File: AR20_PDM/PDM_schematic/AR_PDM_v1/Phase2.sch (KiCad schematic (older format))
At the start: 15 parts, among them Q1 BTS50025-1TAD, U1 INA233

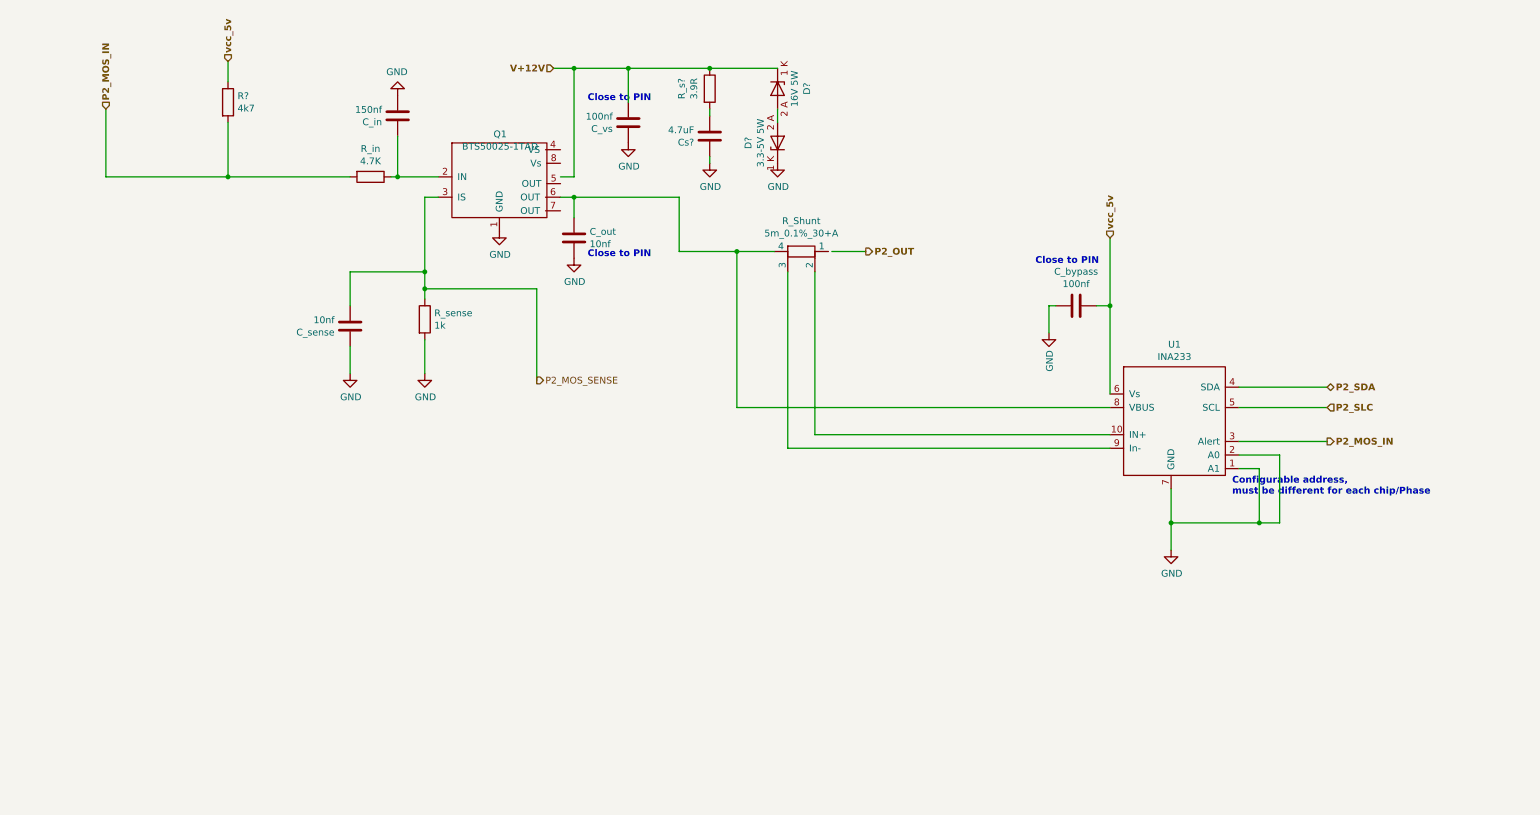
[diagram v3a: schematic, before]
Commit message: Fixed issues, controlled components, BOM, see discription
- added acm symbol
- fixed wrongly faced P-mosfets
- I/O expander now sinks led instead of source
- Bill of material mostly done
- Correct address for INA233 chips.
- Now 4 diodes serves as flyback for all mosfets
- Corrected naming scheme for compmonents (everything is not fixed yet)
- Fixed some labels
- altso some minor changes
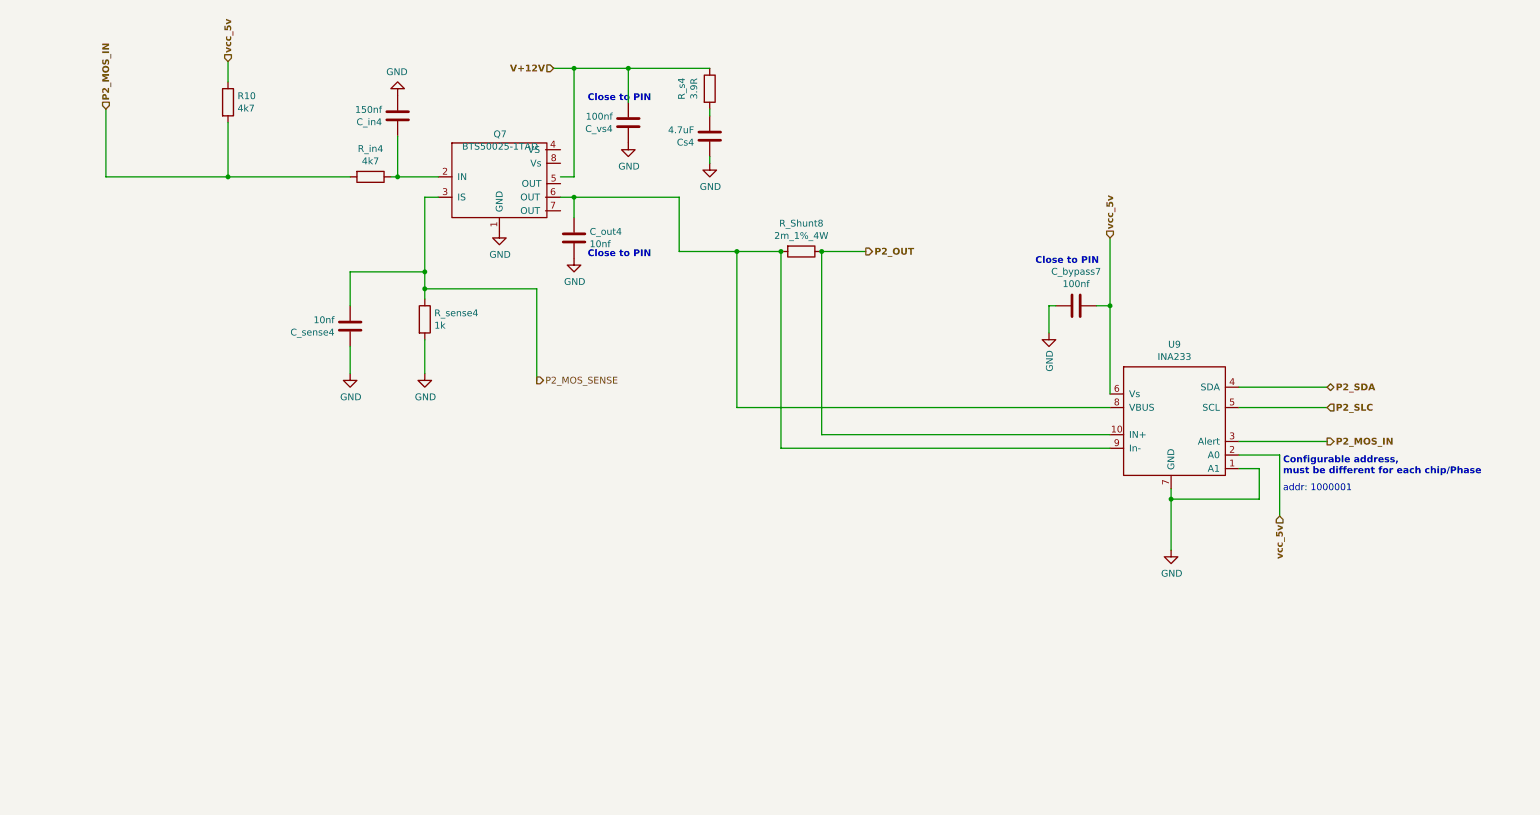
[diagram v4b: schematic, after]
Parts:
- removed C_in: 150nf, symbol AR20_PDM_v1-rescue:C-Device
- removed C_out, C_sense: 10nf, symbol AR20_PDM_v1-rescue:C-Device
- removed C_vs: 100nf, symbol AR20_PDM_v1-rescue:C-Device
- removed Cs?: 4.7uF, symbol AR20_PDM_v1-rescue:C-Device
- removed D?: 3.3-5V 5W, symbol AR20_PDM_v1-rescue:D_Zener-Device
- removed D?: 16V 5W, symbol AR20_PDM_v1-rescue:D_Zener-Device
- removed Q1: BTS50025-1TAD, symbol AR20_PDM_v1-rescue:BTS50025-1TAD
- removed R?: 4k7, symbol AR20_PDM_v1-rescue:R-Device
- removed R_Shunt: 5m_0.1%_30+A, symbol AR20_PDM_v1-rescue:R_Shunt-Device
- removed R_in: 4.7K, symbol AR20_PDM_v1-rescue:R-Device
- removed R_s?: 3.9R, symbol AR20_PDM_v1-rescue:R-Device
- removed R_sense: 1k, symbol AR20_PDM_v1-rescue:R-Device
- removed U1: INA233, symbol AR20_PDM_v1-rescue:INA233
- added C_in4: 150nf, Capacitor_SMD:C_0603_1608Metric, symbol AR20_PDM_v1-rescue:C-Device
- added C_out4, C_sense4: 10nf, Capacitor_SMD:C_0603_1608Metric, symbol AR20_PDM_v1-rescue:C-Device
- added C_vs4: 100nf, Capacitor_SMD:C_0603_1608Metric, symbol AR20_PDM_v1-rescue:C-Device
- added Cs4: 4.7uF, Capacitor_SMD:C_1206_3216Metric, symbol AR20_PDM_v1-rescue:C-Device
- added Q7: BTS50025-1TAD, symbol AR20_PDM_v1-rescue:BTS50025-1TAD
- added R10, R_in4: 4k7, symbol AR20_PDM_v1-rescue:R-Device
- added R_Shunt8: 2m_1%_4W, symbol AR20_PDM_v1-rescue:R-Device
- added R_s4: 3.9R, symbol AR20_PDM_v1-rescue:R-Device
- added R_sense4: 1k, symbol AR20_PDM_v1-rescue:R-Device
- added U9: INA233, symbol AR20_PDM_v1-rescue:INA233
- C_bypass7: renamed from C_bypass; footprint (none) -> Capacitor_SMD:C_0603_1608Metric
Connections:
- wire segments 57 -> 54
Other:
- note added: "addr: 1000001"

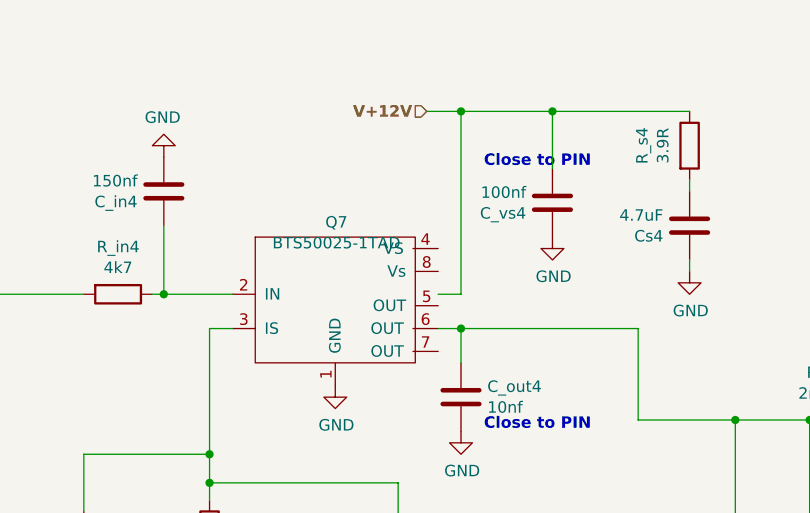
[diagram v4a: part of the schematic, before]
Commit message: PCB design, and issue fixing, work in progress
- Error fixed: Mux mosfet resistor change to ground
- Open drain output added on phase 6, for engine blipping purpose
- Most of pcb symbols and footprints are finished, including main connector
- PCB is change from 1oz to 2oz copper layer, for easier routing.
- Basic Draft of pcb is done, for now.
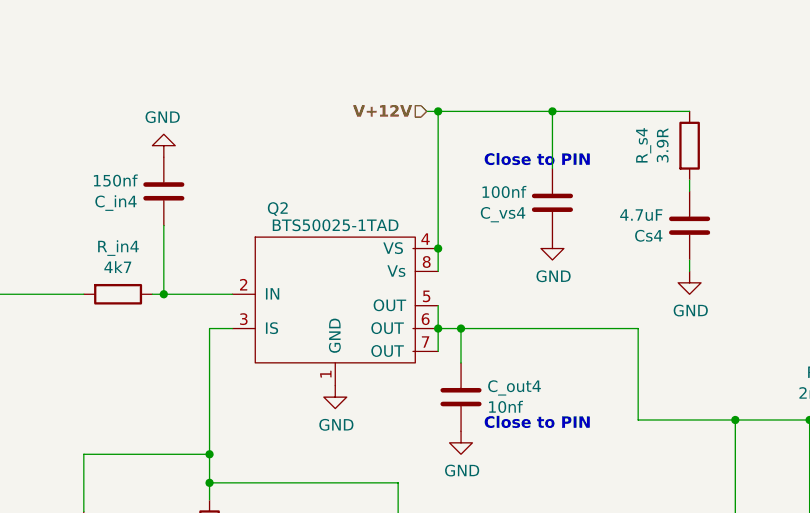
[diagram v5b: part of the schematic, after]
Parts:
- Q2: renamed from Q7; footprint (none) -> AR_PDM_v1:BTS500xx
- R10, R_in4, R_s4, R_sense4: footprint (none) -> Resistor_SMD:R_0603_1608Metric
- R_Shunt8: footprint (none) -> Resistor_SMD:R_2512_6332Metric
- U9: footprint (none) -> AR_PDM_v1:INA233
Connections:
- net V+12V: now also Q2.4 (VS), Q2.8 (Vs)
- net at C_out4.1, Q2.6 (OUT), R_Shunt8.2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: now also Q2.5 (OUT), Q2.7 (OUT)
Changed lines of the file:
@@
 F 0 "R_in4" V 3093 2400 50  0000 C CNN
 F 1 "4k7" V 3184 2400 50  0000 C CNN
-F 2 "" V 3230 2400 50  0001 C CNN
+F 2 "Resistor_SMD:R_0603_1608Metric" V 3230 2400 50  0001 C CNN
 F 3 "~" H 3300 2400 50  0001 C CNN
 	1    3300 2400
@@
 F 0 "R10" H 2320 1896 50  0000 L CNN
 F 1 "4k7" H 2320 1805 50  0000 L CNN
-F 2 "" V 2180 1850 50  0001 C CNN
+F 2 "Resistor_SMD:R_0603_1608Metric" V 2180 1850 50  0001 C CNN
 F 3 "~" H 2250 1850 50  0001 C CNN
 	1    2250 1850
@@
 AR Path="/5E0E594B/5E21B7FD" Ref="Q?"  Part="1"
 AR Path="/5E0E607C/5E21B7FD" Ref="Q?"  Part="1"
-AR Path="/5E0FB5C8/5E21B7FD" Ref="Q7"  Part="1"
+AR Path="/5E0FB5C8/5E21B7FD" Ref="Q2"  Part="1"
 AR Path="/5E0FBBBD/5E21B7FD" Ref="Q?"  Part="1"
 AR Path="/5E0FC3A2/5E21B7FD" Ref="Q?"  Part="1"
@@
 AR Path="/5E0FDCCC/5E21B7FD" Ref="Q?"  Part="1"
 AR Path="/5E10174B/5E21B7FD" Ref="Q?"  Part="1"
-F 0 "Q7" H 4255 3215 50  0000 C CNN
-F 1 "BTS50025-1TAD" H 4255 3124 50  0000 C CNN
-F 2 "" H 4250 2650 50  0001 C CNN
+F 0 "Q2" H 4000 3275 50  0000 C CNN
+F 1 "BTS50025-1TAD" H 4250 3200 50  0000 C CNN
+F 2 "AR_PDM_v1:BTS500xx" H 4250 2650 50  0001 C CNN
 F 3 "" H 4250 2650 50  0001 C CNN
 	1    4250 2650
@@
 F 0 "U9" H 9225 4465 50  0000 C CNN
 F 1 "INA233" H 9225 4374 50  0000 C CNN
-F 2 "" H 9200 4050 50  0001 C CNN
+F 2 "AR_PDM_v1:INA233" H 9200 4050 50  0001 C CNN
 F 3 "" H 9200 4050 50  0001 C CNN
 	1    9200 4050
@@
 Wire Wire Line
 	3700 3100 3700 3225
-Wire Wire Line
-	4700 2400 4800 2400
-Wire Wire Line
-	4800 2400 4800 1600
-Wire Wire Line
-	4800 1600 4650 1600
 Text HLabel 2250 1550 1    50   Input ~ 10
 vcc_5v
@@
 F 0 "R_s4" V 5593 1750 50  0000 C CNN
 F 1 "3.9R" V 5684 1750 50  0000 C CNN
-F 2 "" V 5730 1750 50  0001 C CNN
+F 2 "Resistor_SMD:R_0603_1608Metric" V 5730 1750 50  0001 C CNN
 F 3 "~" H 5800 1750 50  0001 C CNN
 	1    5800 1750
@@
 Wire Wire Line
 	5200 1600 5800 1600
-Wire Wire Line
-	4800 1600 5200 1600
-Connection ~ 4800 1600
 Connection ~ 5200 1600
 Text HLabel 1350 1900 1    50   Input ~ 10
@@
 F 0 "R_sense4" H 3770 3496 50  0000 L CNN
 F 1 "1k" H 3770 3405 50  0000 L CNN
-F 2 "" V 3630 3450 50  0001 C CNN
+F 2 "Resistor_SMD:R_0603_1608Metric" V 3630 3450 50  0001 C CNN
 F 3 "~" H 3700 3450 50  0001 C CNN
 	1    3700 3450
@@
 F 0 "R_Shunt8" V 6268 2950 50  0000 C CNN
 F 1 "2m_1%_4W" V 6359 2950 50  0000 C CNN
-F 2 "" V 6405 2950 50  0001 C CNN
+F 2 "Resistor_SMD:R_2512_6332Metric" V 6405 2950 50  0001 C CNN
 F 3 "~" H 6475 2950 50  0001 C CNN
 	1    6475 2950
@@
 Text HLabel 10000 4900 3    50   Input ~ 10
 vcc_5v
+Wire Wire Line
+	4650 1600 4700 1600
+Wire Wire Line
+	4700 2300 4700 2200
+Wire Wire Line
+	4700 2200 4700 1600
+Connection ~ 4700 2200
+Connection ~ 4700 1600
+Wire Wire Line
+	4700 1600 5200 1600
+Connection ~ 4700 2550
+Wire Wire Line
+	4700 2450 4700 2550
+Wire Wire Line
+	4700 2650 4700 2550
 $EndSCHEMATC

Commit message: PCB Design, Work in progress
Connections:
- net P2_Shunt: now reaches C_out4.1, Q2.5 (OUT), Q2.6 (OUT), Q2.7 (OUT), R_Shunt8.2, U9.8 (VBUS), U9.9 (In-)
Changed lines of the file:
@@
 $Descr A4 11693 8268
 encoding utf-8
-Sheet 8 13
+Sheet 7 13
 Title ""
 Date ""
@@
 Wire Wire Line
 	4700 2650 4700 2550
+Wire Wire Line
+	6000 2950 6000 2825
+Text HLabel 6000 2825 1    50   Input ~ 0
+P2_Shunt
 $EndSCHEMATC

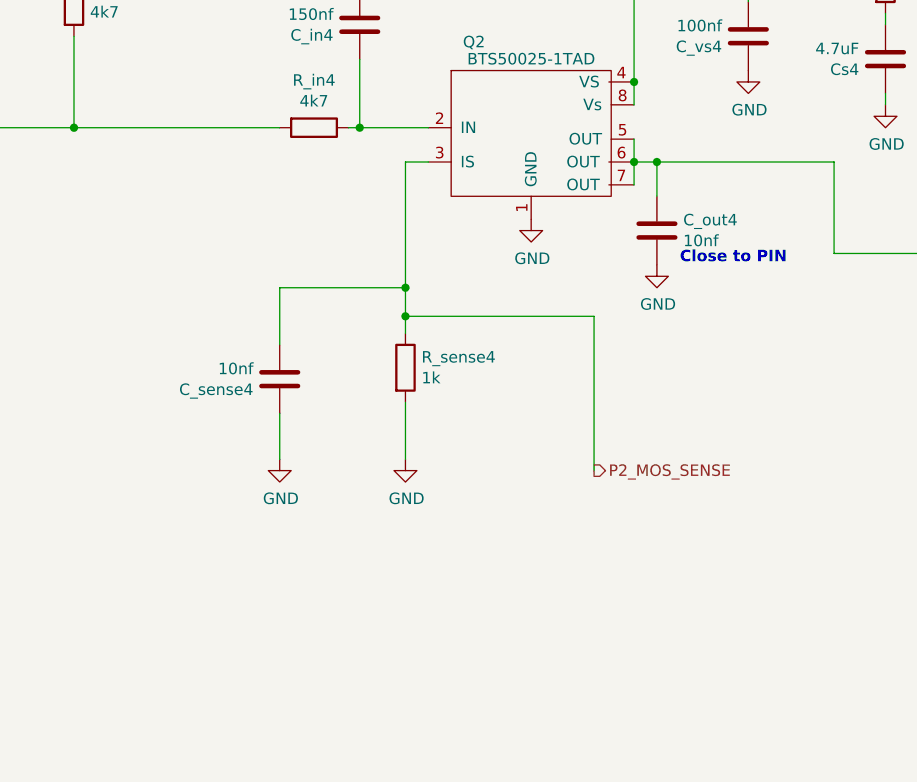
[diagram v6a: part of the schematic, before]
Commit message: PCB Design,  minor schematics changes, work in progress, see description
- Removed mos sense caps and resistors accept one, 
since only one measurement can be done, at a time.
- added mos sens protection resistors on each line, to protect mux mosfets and micro controller. 
- Routing plan mostly finalized, some of the traces are just proof of concept.
those needs to be routed nicely.
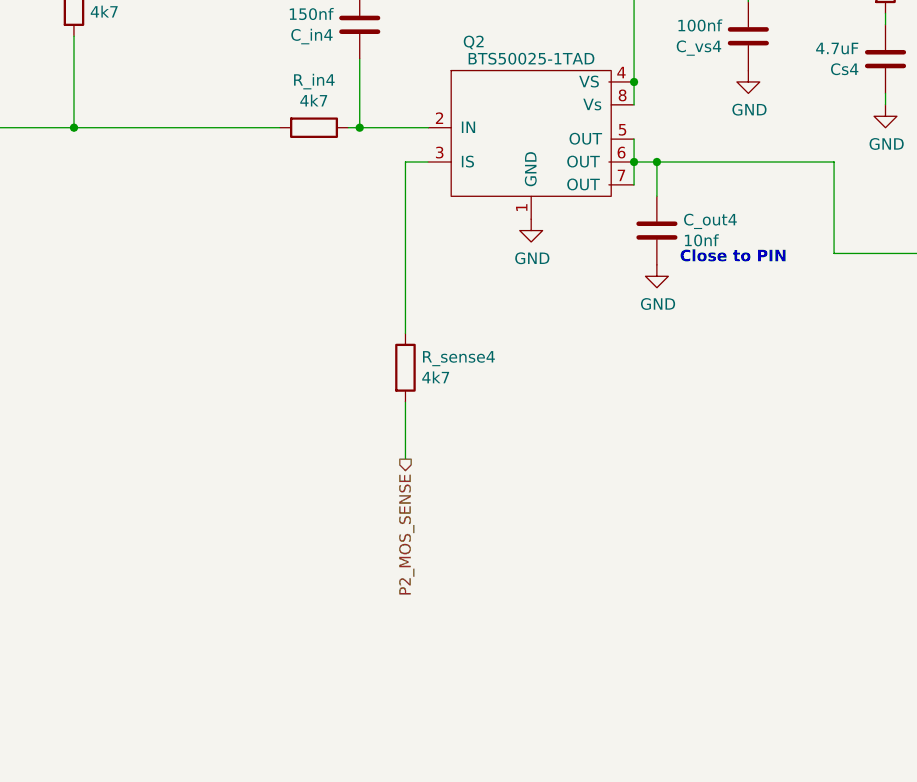
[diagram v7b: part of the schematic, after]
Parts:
- removed C_sense4: 10nf, Capacitor_SMD:C_0603_1608Metric, symbol AR20_PDM_v1-rescue:C-Device
- R_sense4: value 1k -> 4k7
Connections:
- net GND: no longer R_sense4.2
- net P2_MOS_SENSE: now also R_sense4.2; no longer Q2.3 (IS), R_sense4.1
- new net: Q2.3 (IS), R_sense4.1
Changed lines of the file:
@@
-$EndComp
-$Comp
-L AR20_PDM_v1-rescue:GND-power #PWR?
-U 1 1 5DAAC1EF
-P 3700 3850
-AR Path="/5DA89415/5DAAC1EF" Ref="#PWR?"  Part="1"
-AR Path="/5DEB10A1/5DAAC1EF" Ref="#PWR?"  Part="1"
-AR Path="/5DEB20EA/5DAAC1EF" Ref="#PWR?"  Part="1"
-AR Path="/5E0E4725/5DAAC1EF" Ref="#PWR?"  Part="1"
-AR Path="/5E0E4A93/5DAAC1EF" Ref="#PWR?"  Part="1"
-AR Path="/5E0E4EB5/5DAAC1EF" Ref="#PWR?"  Part="1"
-AR Path="/5E0E5304/5DAAC1EF" Ref="#PWR?"  Part="1"
-AR Path="/5E0E594B/5DAAC1EF" Ref="#PWR?"  Part="1"
-AR Path="/5E0E607C/5DAAC1EF" Ref="#PWR?"  Part="1"
-AR Path="/5E0FB5C8/5DAAC1EF" Ref="#PWR065"  Part="1"
-AR Path="/5E0FBBBD/5DAAC1EF" Ref="#PWR?"  Part="1"
-AR Path="/5E0FC3A2/5DAAC1EF" Ref="#PWR?"  Part="1"
-AR Path="/5E0FCFDC/5DAAC1EF" Ref="#PWR?"  Part="1"
-AR Path="/5E0FDCCC/5DAAC1EF" Ref="#PWR?"  Part="1"
-AR Path="/5E10174B/5DAAC1EF" Ref="#PWR?"  Part="1"
-F 0 "#PWR065" H 3700 3600 50  0001 C CNN
-F 1 "GND" H 3705 3677 50  0000 C CNN
-F 2 "" H 3700 3850 50  0001 C CNN
-F 3 "" H 3700 3850 50  0001 C CNN
-	1    3700 3850
-	1    0    0    -1
 $EndComp
 $Comp
@@
 $EndComp
 Wire Wire Line
-	3700 2550 3700 3100
-Wire Wire Line
 	3700 2550 3800 2550
 Wire Wire Line
@@
 Wire Wire Line
 	9700 4450 10000 4450
-$Comp
-L AR20_PDM_v1-rescue:GND-power #PWR?
-U 1 1 5E21B84D
-P 3150 3850
-AR Path="/5DA89415/5E21B84D" Ref="#PWR?"  Part="1"
-AR Path="/5DEB10A1/5E21B84D" Ref="#PWR?"  Part="1"
-AR Path="/5DEB20EA/5E21B84D" Ref="#PWR?"  Part="1"
-AR Path="/5E0E4725/5E21B84D" Ref="#PWR?"  Part="1"
-AR Path="/5E0E4A93/5E21B84D" Ref="#PWR?"  Part="1"
-AR Path="/5E0E4EB5/5E21B84D" Ref="#PWR?"  Part="1"
-AR Path="/5E0E5304/5E21B84D" Ref="#PWR?"  Part="1"
-AR Path="/5E0E594B/5E21B84D" Ref="#PWR?"  Part="1"
-AR Path="/5E0E607C/5E21B84D" Ref="#PWR?"  Part="1"
-AR Path="/5E0FB5C8/5E21B84D" Ref="#PWR063"  Part="1"
-AR Path="/5E0FBBBD/5E21B84D" Ref="#PWR?"  Part="1"
-AR Path="/5E0FC3A2/5E21B84D" Ref="#PWR?"  Part="1"
-AR Path="/5E0FCFDC/5E21B84D" Ref="#PWR?"  Part="1"
-AR Path="/5E0FDCCC/5E21B84D" Ref="#PWR?"  Part="1"
-AR Path="/5E10174B/5E21B84D" Ref="#PWR?"  Part="1"
-F 0 "#PWR063" H 3150 3600 50  0001 C CNN
-F 1 "GND" H 3155 3677 50  0000 C CNN
-F 2 "" H 3150 3850 50  0001 C CNN
-F 3 "" H 3150 3850 50  0001 C CNN
-	1    3150 3850
-	1    0    0    -1
-$EndComp
-$Comp
-L AR20_PDM_v1-rescue:C-Device C_sense?
-U 1 1 5E21B853
-P 3150 3500
-AR Path="/5DA89415/5E21B853" Ref="C_sense?"  Part="1"
-AR Path="/5DEB10A1/5E21B853" Ref="C_sense?"  Part="1"
-AR Path="/5DEB20EA/5E21B853" Ref="C_sense?"  Part="1"
-AR Path="/5E0E4725/5E21B853" Ref="C_sense?"  Part="1"
-AR Path="/5E0E4A93/5E21B853" Ref="C_sense?"  Part="1"
-AR Path="/5E0E4EB5/5E21B853" Ref="C_sense?"  Part="1"
-AR Path="/5E0E5304/5E21B853" Ref="C_sense?"  Part="1"
-AR Path="/5E0E594B/5E21B853" Ref="C_sense?"  Part="1"
-AR Path="/5E0E607C/5E21B853" Ref="C_sense?"  Part="1"
-AR Path="/5E0FB5C8/5E21B853" Ref="C_sense4"  Part="1"
-AR Path="/5E0FBBBD/5E21B853" Ref="C_sense?"  Part="1"
-AR Path="/5E0FC3A2/5E21B853" Ref="C_sense?"  Part="1"
-AR Path="/5E0FCFDC/5E21B853" Ref="C_sense?"  Part="1"
-AR Path="/5E0FDCCC/5E21B853" Ref="C_sense?"  Part="1"
-AR Path="/5E10174B/5E21B853" Ref="C_sense?"  Part="1"
-F 0 "C_sense4" H 3265 3546 50  0000 L CNN
-F 1 "10nf" H 3265 3455 50  0000 L CNN
-F 2 "Capacitor_SMD:C_0603_1608Metric" H 3188 3350 50  0001 C CNN
-F 3 "~" H 3150 3500 50  0001 C CNN
-	1    3150 3500
-	-1   0    0    1
-$EndComp
 Wire Wire Line
 	3450 2400 3500 2400
@@
 Text Notes 8200 3050 0    50   ~ 10
 Close to PIN
-Wire Wire Line
-	3150 3100 3150 3350
-Wire Wire Line
-	3150 3650 3150 3850
-Wire Wire Line
-	3150 3100 3700 3100
-Connection ~ 3700 3100
-Wire Wire Line
-	3700 3100 3700 3225
 Text HLabel 2250 1550 1    50   Input ~ 10
 vcc_5v
@@
 AR Path="/5E10174B/5E21B872" Ref="R_sense?"  Part="1"
 F 0 "R_sense4" H 3770 3496 50  0000 L CNN
-F 1 "1k" H 3770 3405 50  0000 L CNN
+F 1 "4k7" H 3770 3405 50  0000 L CNN
 F 2 "Resistor_SMD:R_0603_1608Metric" V 3630 3450 50  0001 C CNN
 F 3 "~" H 3700 3450 50  0001 C CNN
@@
 Wire Wire Line
 	6325 4400 8750 4400
-Wire Wire Line
-	3700 3225 4525 3225
-Wire Wire Line
-	4525 3225 4525 3900
-Connection ~ 3700 3225
-Wire Wire Line
-	3700 3225 3700 3300
-Text HLabel 4525 3900 2    50   Output ~ 0
+Text HLabel 3700 3850 3    50   Output ~ 0
 P2_MOS_SENSE
 Wire Wire Line
@@
 Text HLabel 6000 2825 1    50   Input ~ 0
 P2_Shunt
+Wire Wire Line
+	3700 2550 3700 3300
 $EndSCHEMATC
